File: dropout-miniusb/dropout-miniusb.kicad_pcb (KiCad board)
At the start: 2 copper layers, 75 x 94.1 mm, 45 parts, among them SW1 Rotary_Encoder_Switch, SW2 SW_Push, U1 ProMicro

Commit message: firmware
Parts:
- added C1: 10nF, Capacitor_SMD:C_0805_2012Metric_Pad1.15x1.40mm_HandSolder, B.Cu at (156.0, 60.1)
- added C2: 10nF, Capacitor_SMD:C_0805_2012Metric_Pad1.15x1.40mm_HandSolder, B.Cu at (156.0, 57.4)
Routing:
- net ROT-B: track 27.3 -> 32.4 mm
- net ROT-A: track 29.2 -> 32.9 mm

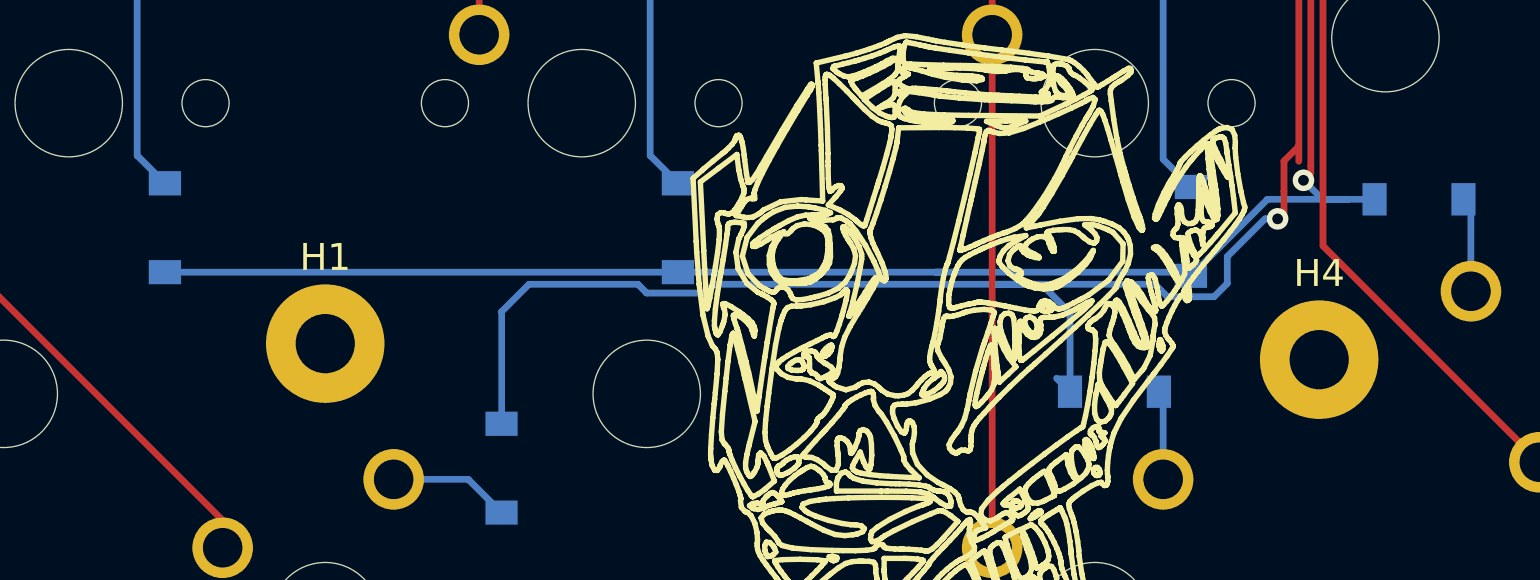
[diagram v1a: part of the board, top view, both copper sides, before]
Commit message: move screws away from stabs
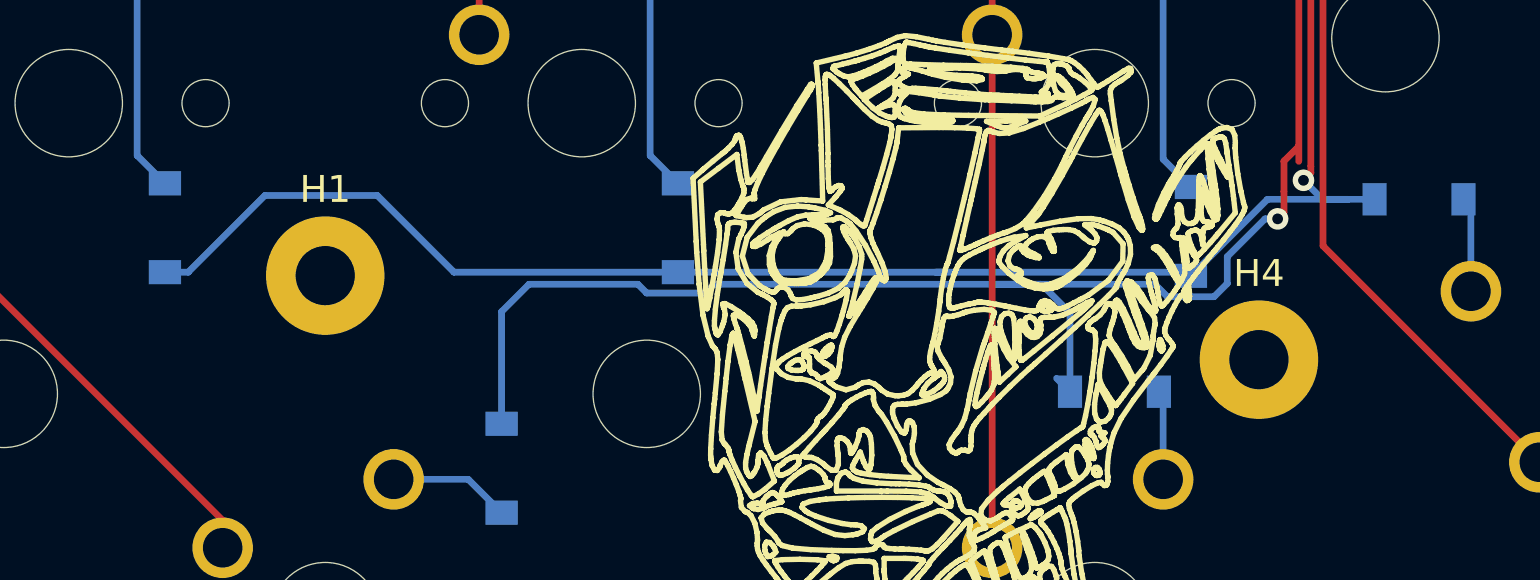
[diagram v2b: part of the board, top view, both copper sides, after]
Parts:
- moved H1 2.53 mm to (111.2, 123.2)
- moved H4 2.24 mm to (145.9, 126.4)
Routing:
- net ROW3: track 105.2 -> 107.5 mm

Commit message: cleanup
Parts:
- moved D13 45.0 mm to (188.3, 120.2)
- moved D1 45.0 mm to (152.2, 55.8)
- moved J-ISP1 45.0 mm to (153.0, 105.9)
- moved C1 45.0 mm to (201.0, 59.9)
- moved C2 45.0 mm to (201.0, 57.2)
- moved D11 45.0 mm to (187.7, 83.2)
- moved D12 45.0 mm to (187.7, 102.2)
- moved D15 45.0 mm to (198.0, 52.9)
- moved D16 45.0 mm to (206.8, 83.2)
- moved D17 45.0 mm to (206.8, 102.2)
- moved D18 45.0 mm to (196.8, 120.2)
- moved D2 45.0 mm to (151.4, 82.1)
- moved D3 45.0 mm to (149.6, 102.3)
- moved D4 45.0 mm to (150.2, 121.3)
- moved D5 45.0 mm to (162.7, 130.2)
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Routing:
- net Net-(D14-Pad2): track 3.32 -> 5.64 mm
- net ROW1: track 110.7 -> 108.5 mm
- net ROW4: track 99.5 -> 97.8 mm
- net Net-(D13-Pad2): track 8.62 -> 7.43 mm
- net ROW3: track 107.5 -> 106.4 mm
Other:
- board size 75 x 94.1 mm -> 75.1 x 94.2 mm
- board text added: "dropout by enochau rev0.2"
- board text removed: "dropout by enochau rev0.1"
